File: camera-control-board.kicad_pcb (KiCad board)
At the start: 6 copper layers, 90 x 96 mm, 51 parts, among them J1 DF12NB-36DS-0.5V_51_, J2 10104110-0001LF, J3 104031-0811, J4 02x05 M 1.27mm, J5 Conn_01x09, SW1 CAS-120TA, SW3 SW_Push, U1 STM32H743IITx, U2 IS42S32800J-7TLI, U3 W25Q256JVEIQ TR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

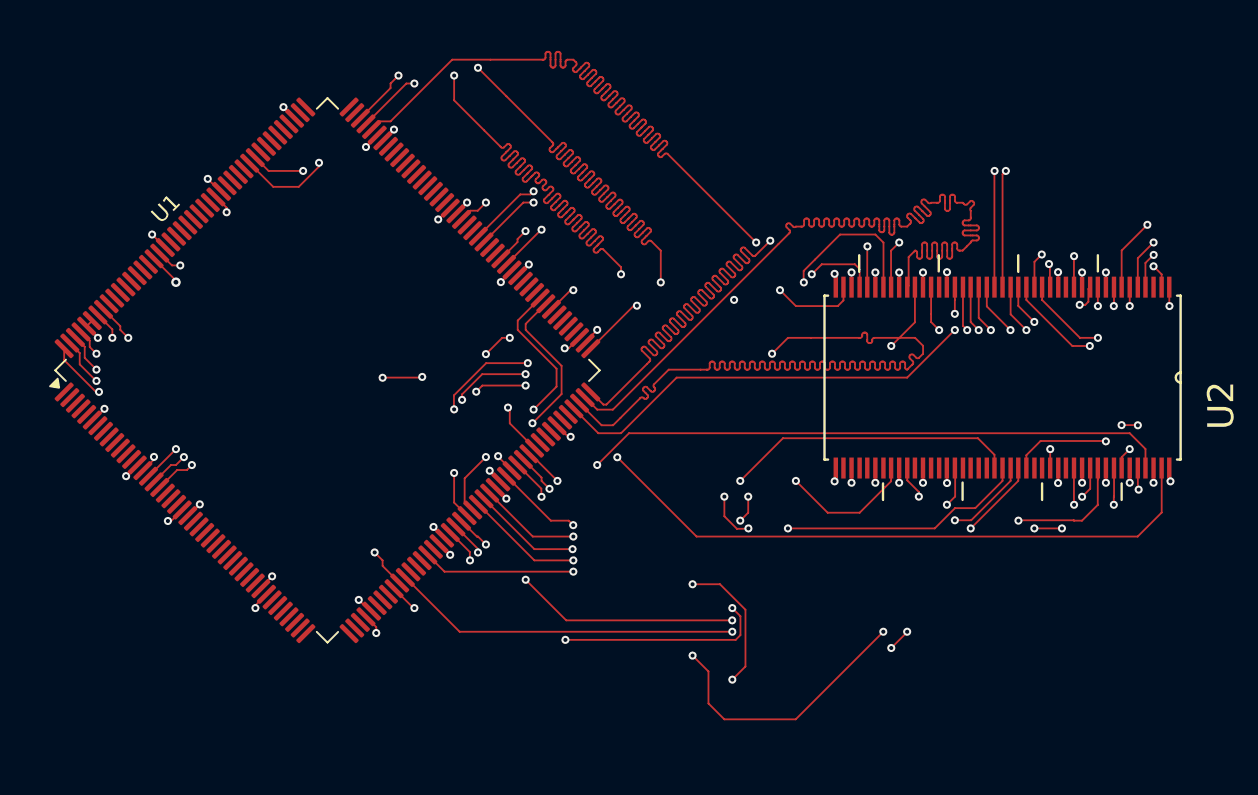
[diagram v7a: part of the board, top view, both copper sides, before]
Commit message: all traces routed, impedance matching fight begins
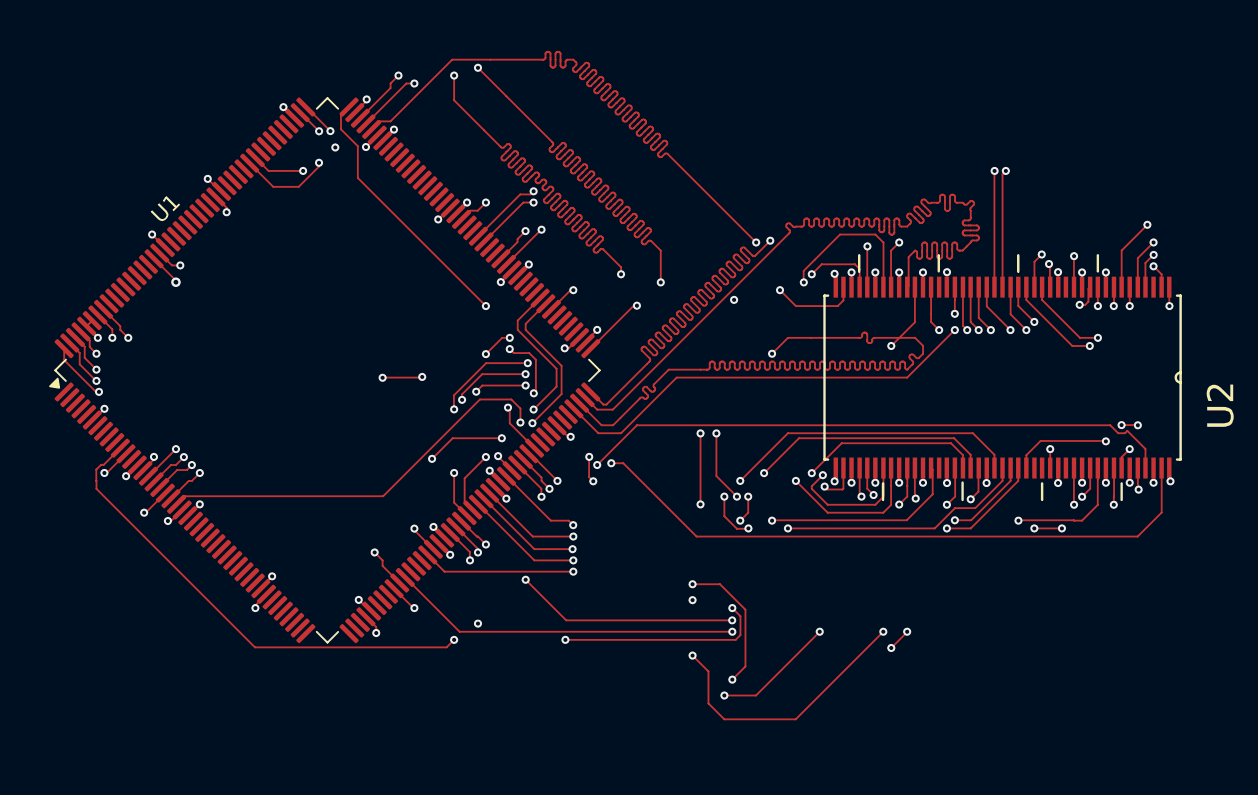
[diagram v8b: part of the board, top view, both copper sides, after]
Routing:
- net /DRAM_D30: track 0.00 -> 65.0 mm, vias 0 -> 2
- net /DRAM_D31: track 0.00 -> 64.8 mm, vias 0 -> 3
- net /DRAM_A3: track 0.00 -> 62.9 mm, vias 0 -> 3
- net /DRAM_A5: track 0.00 -> 59.9 mm, vias 0 -> 2
- net /DRAM_D27: track 0.00 -> 58.0 mm, vias 0 -> 6
- net /DRAM_A4: track 0.00 -> 57.9 mm, vias 0 -> 6
- net /DRAM_A6: track 0.00 -> 49.3 mm, vias 0 -> 4
- net /DRAM_D25: track 0.00 -> 49.1 mm, vias 0 -> 4
- net /DRAM_D26: track 0.00 -> 47.8 mm, vias 0 -> 2
- net /DRAM_D24: track 0.00 -> 47.2 mm, vias 0 -> 3
- net /DRAM_D28: track 60.2 -> 61.4 mm
- net /DRAM_D29: track 62.0 -> 61.4 mm
- net /DRAM_DQM1: track 64.9 -> 65.5 mm
- net /DRAM_D14: track 51.8 -> 52.4 mm
